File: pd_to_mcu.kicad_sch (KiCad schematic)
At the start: 0 parts

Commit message: updated UPD module
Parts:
- added C? (x2): 1u, symbol Device:C_Small
- added C? (x2): 2.2u, symbol Device:C_Small
- added D? (x2): D_TVS, Diode_SMD:D_1206_3216Metric_Pad1.42x1.75mm_HandSolder, symbol Device:D_TVS
- added J?: USB_C_Receptacle_USB2.0, symbol Connector:USB_C_Receptacle_USB2.0
- added R? (x3): R_US, symbol Device:R_US
- added U?: UPD350B28-QFN, symbol UPD:UPD350B28-QFN
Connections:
- new net: D?.1 (A1), J?.A6 (D+), J?.B6 (D+)
- new net: D?.1 (A1), J?.A7 (D-), J?.B7 (D-)
- new net: R?.2, U?. (VSW)
- new net +5V: J?.A4 (VBUS), J?.A9 (VBUS), J?.B4 (VBUS), J?.B9 (VBUS)
- new net 3V3_ALW: C?.2, U?. (VSW)
- new net D+: D?.2 (A2)
- new net D-: D?.2 (A2)
- new net Earth: C?.1, C?.1, C?.1, C?.1, J?.A1 (GND), J?.A12 (GND), J?.B1 (GND), J?.B12 (GND), J?.S1 (SHIELD), R?.1, U?. (VSW)
- new net VBUS: C?.2, R?.2, U?. (VSW)
- new net VBUS_DET: R?.1, R?.2, U?. (VSW)
- new net VDD18_CAP: C?.2, U?. (VSW)
- new net VDD33IO: R?.1, U?. (VSW)
- new net VSW: C?.2, U?. (VSW)

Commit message: update after meeting on tues
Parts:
- removed D? (x2): D_TVS, Diode_SMD:D_1206_3216Metric_Pad1.42x1.75mm_HandSolder, symbol Device:D_TVS
- added R?: R_US, symbol Device:R_US
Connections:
- net +5V is gone; now on net VBUS: J?.A4 (VBUS), J?.A9 (VBUS), J?.B4 (VBUS), J?.B9 (VBUS)
- net D+: now also J?.A6 (D+), J?.B6 (D+)
- net D-: now also J?.A7 (D-), J?.B7 (D-)
- net Earth: now also R?.1
- net CC1: now reaches J?.A5 (CC1)
- net CC1: now also U?. (VSW)
- net CC2: now reaches J?.B5 (CC2)
- net CC2: now also U?. (VSW)
- new net CFG_SEL: R?.2, U?. (VSW)
- new net VCONN: U?. (VSW)
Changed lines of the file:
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@@
+    (stroke (width 0) (type default) (color 0 0 0 0))
+  )
+  (wire (pts (xy 121.92 110.49) (xy 121.92 113.03))
+    (stroke (width 0) (type default) (color 0 0 0 0))
+  )
+  (wire (pts (xy 124.46 110.49) (xy 124.46 113.03))
+    (stroke (width 0) (type default) (color 0 0 0 0))
+  )
+  (wire (pts (xy 127 110.49) (xy 127 113.03))
     (stroke (width 0) (type default) (color 0 0 0 0))
   )
@@
     (stroke (width 0) (type default) (color 0 0 0 0))
   )
+  (wire (pts (xy 132.08 110.49) (xy 132.08 113.03))
+    (stroke (width 0) (type default) (color 0 0 0 0))
+  )
   (wire (pts (xy 144.78 87.63) (xy 147.32 87.63))
     (stroke (width 0) (type default) (color 0 0 0 0))
@@
     (stroke (width 0) (type default) (color 0 0 0 0))
   )
+  (wire (pts (xy 160.02 120.65) (xy 160.02 125.73))
+    (stroke (width 0) (type default) (color 0 0 0 0))
+  )
+  (wire (pts (xy 160.02 133.35) (xy 160.02 137.16))
+    (stroke (width 0) (type default) (color 0 0 0 0))
+  )
   (wire (pts (xy 167.64 74.93) (xy 171.45 74.93))
     (stroke (width 0) (type default) (color 0 0 0 0))
@@
     (stroke (width 0) (type default) (color 0 0 0 0))
   )
-  (wire (pts (xy 231.14 74.93) (xy 238.76 74.93))
-    (stroke (width 0) (type default) (color 0 0 0 0))
-  )
-  (wire (pts (xy 231.14 88.9) (xy 231.14 87.63))
-    (stroke (width 0) (type default) (color 0 0 0 0))
-  )
-  (wire (pts (xy 231.14 90.17) (xy 231.14 88.9))
-    (stroke (width 0) (type default) (color 0 0 0 0))
-  )
-  (wire (pts (xy 231.14 93.98) (xy 231.14 92.71))
-    (stroke (width 0) (type default) (color 0 0 0 0))
-  )
-  (wire (pts (xy 231.14 95.25) (xy 231.14 93.98))
+  (wire (pts (xy 231.14 74.93) (xy 236.22 74.93))
+    (stroke (width 0) (type default) (color 0 0 0 0))
+  )
+  (wire (pts (xy 231.14 80.01) (xy 236.22 80.01))
+    (stroke (width 0) (type default) (color 0 0 0 0))
+  )
+  (wire (pts (xy 231.14 82.55) (xy 236.22 82.55))
+    (stroke (width 0) (type default) (color 0 0 0 0))
+  )
+  (wire (pts (xy 231.14 87.63) (xy 231.14 88.9))
+    (stroke (width 0) (type default) (color 0 0 0 0))
+  )
+  (wire (pts (xy 231.14 88.9) (xy 231.14 90.17))
+    (stroke (width 0) (type default) (color 0 0 0 0))
+  )
+  (wire (pts (xy 231.14 88.9) (xy 233.68 88.9))
+    (stroke (width 0) (type default) (color 0 0 0 0))
+  )
+  (wire (pts (xy 231.14 92.71) (xy 231.14 93.98))
+    (stroke (width 0) (type default) (color 0 0 0 0))
+  )
+  (wire (pts (xy 231.14 93.98) (xy 231.14 95.25))
+    (stroke (width 0) (type default) (color 0 0 0 0))
+  )
+  (wire (pts (xy 231.14 93.98) (xy 233.68 93.98))
     (stroke (width 0) (type default) (color 0 0 0 0))
   )
@@
     )
   )
+  (global_label "CC2" (shape input) (at 121.92 113.03 270) (fields_autoplaced)
+    (effects (font (size 1.27 1.27)) (justify right))
+    (property "Intersheet References" "${INTERSHEET_REFS}" (id 0) (at 121.9994 119.1037 90)
+      (effects (font (size 1.27 1.27)) (justify right) hide)
+    )
+  )
+  (global_label "VCONN" (shape input) (at 124.46 113.03 270) (fields_autoplaced)
+    (effects (font (size 1.27 1.27)) (justify right))
+    (property "Intersheet References" "${INTERSHEET_REFS}" (id 0) (at 124.3806 121.7042 90)
+      (effects (font (size 1.27 1.27)) (justify right) hide)
+    )
+  )
+  (global_label "CC1" (shape input) (at 127 113.03 270) (fields_autoplaced)
+    (effects (font (size 1.27 1.27)) (justify right))
+    (property "Intersheet References" "${INTERSHEET_REFS}" (id 0) (at 127.0794 119.1037 90)
+      (effects (font (size 1.27 1.27)) (justify right) hide)
+    )
+  )
   (global_label "VBUS_DET" (shape input) (at 129.54 113.03 270) (fields_autoplaced)
     (effects (font (size 1.27 1.27)) (justify right))
@@
     )
   )
+  (global_label "CFG_SEL" (shape input) (at 132.08 113.03 270) (fields_autoplaced)
+    (effects (font (size 1.27 1.27)) (justify right))
+    (property "Intersheet References" "${INTERSHEET_REFS}" (id 0) (at 132.0006 123.3371 90)
+      (effects (font (size 1.27 1.27)) (justify right) hide)
+    )
+  )
   (global_label "VDD33IO" (shape input) (at 147.32 87.63 0) (fields_autoplaced)
     (effects (font (size 1.27 1.27)) (justify left))
@@
     )
   )
+  (global_label "CFG_SEL" (shape input) (at 160.02 120.65 90) (fields_autoplaced)
+    (effects (font (size 1.27 1.27)) (justify left))
+    (property "Intersheet References" "${INTERSHEET_REFS}" (id 0) (at 160.0994 110.3429 90)
+      (effects (font (size 1.27 1.27)) (justify left) hide)
+    )
+  )
   (global_label "VBUS_DET" (shape input) (at 171.45 74.93 0) (fields_autoplaced)
     (effects (font (size 1.27 1.27)) (justify left))
@@
     )
   )
-  (global_label "D-" (shape input) (at 238.76 88.9 0) (fields_autoplaced)
-    (effects (font (size 1.27 1.27)) (justify left))
-    (property "Intersheet References" "${INTERSHEET_REFS}" (id 0) (at 88.9 -16.51 0)
-      (effects (font (size 1.27 1.27)) hide)
-    )
-  )
-  (global_label "D+" (shape input) (at 238.76 93.98 0) (fields_autoplaced)
-    (effects (font (size 1.27 1.27)) (justify left))
-    (property "Intersheet References" "${INTERSHEET_REFS}" (id 0) (at 88.9 -16.51 0)
-      (effects (font (size 1.27 1.27)) hide)
-    )
-  )
-  (symbol (lib_id "power:+5V") (at 238.76 74.93 0) (unit 1)
-    (in_bom yes) (on_board yes)
-    (property "Reference" "#PWR?" (id 0) (at 238.76 78.74 0)
-      (effects (font (size 1.27 1.27)) hide)
-    )
-    (property "Value" "+5V" (id 1) (at 239.141 70.5358 0))
-    (property "Footprint" "" (id 2) (at 238.76 74.93 0)
-      (effects (font (size 1.27 1.27)) hide)
-    )
-    (property "Datasheet" "" (id 3) (at 238.76 74.93 0)
-      (effects (font (size 1.27 1.27)) hide)
-    )
-    (pin "1")
+  (global_label "D-" (shape input) (at 233.68 88.9 0) (fields_autoplaced)
+    (effects (font (size 1.27 1.27)) (justify left))
+    (property "Intersheet References" "${INTERSHEET_REFS}" (id 0) (at 83.82 -16.51 0)
+      (effects (font (size 1.27 1.27)) hide)
+    )
+  )
+  (global_label "D+" (shape input) (at 233.68 93.98 0) (fields_autoplaced)
+    (effects (font (size 1.27 1.27)) (justify left))
+    (property "Intersheet References" "${INTERSHEET_REFS}" (id 0) (at 83.82 -16.51 0)
+      (effects (font (size 1.27 1.27)) hide)
+    )
+  )
+  (global_label "VBUS" (shape input) (at 236.22 74.93 0) (fields_autoplaced)
+    (effects (font (size 1.27 1.27)) (justify left))
+    (property "Intersheet References" "${INTERSHEET_REFS}" (id 0) (at 243.4428 74.8506 0)
+      (effects (font (size 1.27 1.27)) (justify left) hide)
+    )
+  )
+  (global_label "CC1" (shape input) (at 236.22 80.01 0) (fields_autoplaced)
+    (effects (font (size 1.27 1.27)) (justify left))
+    (property "Intersheet References" "${INTERSHEET_REFS}" (id 0) (at 242.2937 79.9306 0)
+      (effects (font (size 1.27 1.27)) (justify left) hide)
+    )
+  )
+  (global_label "CC2" (shape input) (at 236.22 82.55 0) (fields_autoplaced)
+    (effects (font (size 1.27 1.27)) (justify left))
+    (property "Intersheet References" "${INTERSHEET_REFS}" (id 0) (at 242.2937 82.4706 0)
+      (effects (font (size 1.27 1.27)) (justify left) hide)
+    )
   )
   (symbol (lib_id "power:Earth") (at 64.77 115.57 0) (unit 1)
@@
     )
     (property "Datasheet" "~" (id 3) (at 137.16 110.49 0)
+      (effects (font (size 1.27 1.27)) hide)
+    )
+    (pin "1")
+  )
+  (symbol (lib_id "power:Earth") (at 160.02 137.16 0) (unit 1)
+    (in_bom yes) (on_board yes) (fields_autoplaced)
+    (property "Reference" "#PWR?" (id 0) (at 160.02 143.51 0)
+      (effects (font (size 1.27 1.27)) hide)
+    )
+    (property "Value" "Earth" (id 1) (at 160.02 140.97 0)
+      (effects (font (size 1.27 1.27)) hide)
+    )
+    (property "Footprint" "" (id 2) (at 160.02 137.16 0)
+      (effects (font (size 1.27 1.27)) hide)
+    )
+    (property "Datasheet" "~" (id 3) (at 160.02 137.16 0)
       (effects (font (size 1.27 1.27)) hide)
     )
@@
     )
     (property "Datasheet" "~" (id 3) (at 110.49 83.82 0)
+      (effects (font (size 1.27 1.27)) hide)
+    )
+    (pin "1")
+    (pin "2")
+  )
+  (symbol (lib_id "Device:R_US") (at 160.02 129.54 180) (unit 1)
+    (in_bom yes) (on_board yes) (fields_autoplaced)
+    (property "Reference" "R?" (id 0) (at 161.6711 128.6315 0)
+      (effects (font (size 1.27 1.27)) (justify right))
+    )
+    (property "Value" "R_US" (id 1) (at 161.6711 131.4066 0)
+      (effects (font (size 1.27 1.27)) (justify right))
+    )
+    (property "Footprint" "" (id 2) (at 159.004 129.286 90)
+      (effects (font (size 1.27 1.27)) hide)
+    )
+    (property "Datasheet" "~" (id 3) (at 160.02 129.54 0)
       (effects (font (size 1.27 1.27)) hide)
     )
@@
       (effects (font (size 1.27 1.27)) hide)
     )
-    (pin "1")
-    (pin "2")
-  )
-  (symbol (lib_id "Device:D_TVS") (at 234.95 88.9 0) (unit 1)
-    (in_bom yes) (on_board yes)
-    (property "Reference" "D?" (id 0) (at 234.95 83.3882 0))
-    (property "Value" "D_TVS" (id 1) (at 234.95 85.6996 0))
-    (property "Footprint" "Diode_SMD:D_1206_3216Metric_Pad1.42x1.75mm_HandSolder" (id 2) (at 234.95 88.9 0)
-      (effects (font (size 1.27 1.27)) hide)
-    )
-    (property "Datasheet" "~" (id 3) (at 234.95 88.9 0)
-      (effects (font (size 1.27 1.27)) hide)
-    )
-    (pin "1")
-    (pin "2")
-  )
-  (symbol (lib_id "Device:D_TVS") (at 234.95 93.98 0) (unit 1)
-    (in_bom yes) (on_board yes)
-    (property "Reference" "D?" (id 0) (at 234.95 96.52 0))
-    (property "Value" "D_TVS" (id 1) (at 234.95 99.06 0))
-    (property "Footprint" "Diode_SMD:D_1206_3216Metric_Pad1.42x1.75mm_HandSolder" (id 2) (at 234.95 93.98 0)
-      (effects (font (size 1.27 1.27)) hide)
-    )
-    (property "Datasheet" "~" (id 3) (at 234.95 93.98 0)
-      (effects (font (size 1.27 1.27)) hide)
-    )

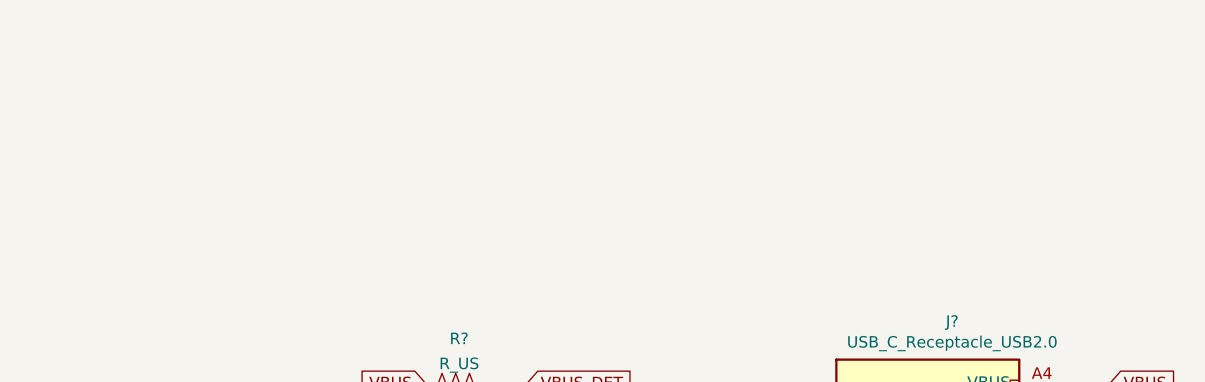
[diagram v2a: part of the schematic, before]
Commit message: added TODOs and comments
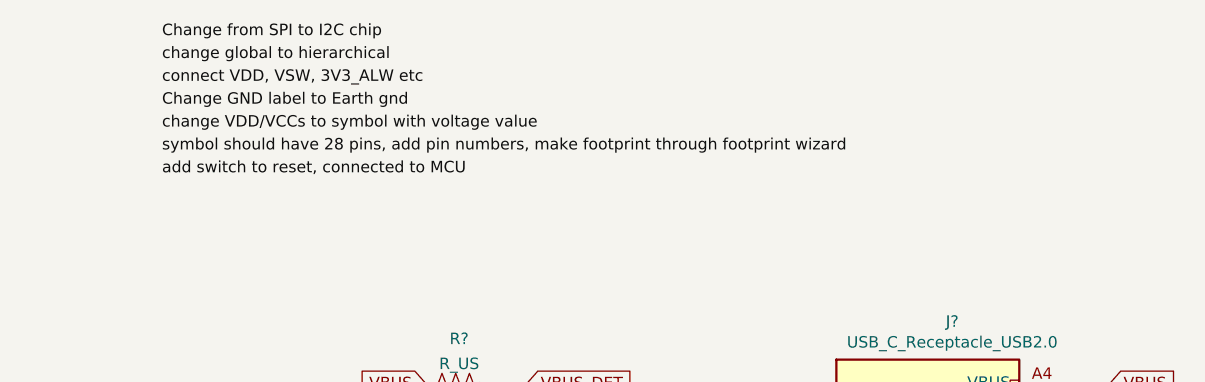
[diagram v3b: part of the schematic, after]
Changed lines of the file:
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@@
     (stroke (width 0) (type default) (color 0 0 0 0))
+  )
+  (label "Change from SPI to I2C chip" (at 130.81 36.83 0)
+    (effects (font (size 1.27 1.27)) (justify left bottom))
+  )
+  (label "change global to hierarchical" (at 130.81 39.37 0)
+    (effects (font (size 1.27 1.27)) (justify left bottom))
+  )
+  (label "connect VDD, VSW, 3V3_ALW etc" (at 130.81 41.91 0)
+    (effects (font (size 1.27 1.27)) (justify left bottom))
+  )
+  (label "Change GND label to Earth gnd" (at 130.81 44.45 0)
+    (effects (font (size 1.27 1.27)) (justify left bottom))
+  )
+  (label "change VDD{slash}VCCs to symbol with voltage value"
+    (at 130.81 46.99 0)
+    (effects (font (size 1.27 1.27)) (justify left bottom))
+  )
+  (label "symbol should have 28 pins, add pin numbers, make footprint through footprint wizard"
+    (at 130.81 49.53 0)
+    (effects (font (size 1.27 1.27)) (justify left bottom))
+  )
+  (label "add switch to reset, connected to MCU" (at 130.81 52.07 0)
+    (effects (font (size 1.27 1.27)) (justify left bottom))
   )
   (global_label "VDD18_CAP" (shape input) (at 74.93 81.28 0) (fields_autoplaced)

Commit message: updated UPD
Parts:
- removed C?: 2.2u, symbol Device:C_Small
- removed C?: 1u, symbol Device:C_Small
- U?: value UPD350B28-QFN -> UPD350A28-QFN
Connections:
- net CC1: now also U?.3 (CC1); no longer U?. (VSW)
- net CC2: now also U?.1 (CC2); no longer U?. (VSW)
- net CFG_SEL: now also U?.5 (CFG_SEL); no longer U?. (VSW)
- net Earth: now also U?.7 (PWR_DN); no longer U?. (VSW)
- net VBUS: now also U?.10 (3V3_VBUS), U?.8 (3V3_ALW); no longer U?. (VSW)
- net VBUS_DET: now also U?.4 (VBUS_DET); no longer U?. (VSW)
- net VCONN: now also U?.2 (VS); no longer U?. (VSW)
- net VSW: now also U?.11 (VDD18_CAP), U?.9 (VSW); no longer U?. (VSW)
- net at R?.2: no longer U?. (VSW)
- removed net 3V3_ALW: U?. (VSW)
- removed net VDD18_CAP: U?. (VSW)
- net VDD33IO renamed 3V3
- net 3V3: now also U?.12 (VDD33IO); no longer U?. (VSW)
- new net I2C_CLK_3V3: U?.14 (VDD_I2C)
- new net I2C_DAT_3V3: U?.13 (I2C_DAT)
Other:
- added sheet level_shifter_bidirectional (level_shifter_bidirectional_sch.kicad_sch)
- added sheet level_shifter_bidirectional1 (level_shifter_bidirectional_sch.kicad_sch)
- moved on the sheet: C?, J?

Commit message: updated schematic
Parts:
- added C? (x2): 1u, symbol Device:C_Small
- added D? (x3): LED_Small, symbol Device:LED_Small
- added U?: TPS7A0518PDBV, Package_TO_SOT_SMD:SOT-23-5, symbol Regulator_Linear:TPS7A0518PDBV
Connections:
- net Earth: now also C?.1, C?.1, D?.1 (K), D?.1 (K), D?.1 (K), U?.2 (GND)
- net I2C_CLK_3V3: now also U?.15 (I2C_CLK); no longer U?.14 (VDD_I2C)
- net +1V8: now reaches U?.20 (VDD18)
- net +1V8: now also C?.2, U?.5 (OUT)
- net ~{PD_IRQ}: now reaches U?.21 (IRQ_N)
- net ~{PD_RESET}: now reaches U?.22 (RESET_N)
- net ~{PD_RESET}: now also R?.2
- net at U?.26 (GPIO7): now also D?.2 (A)
- net at U?.27 (GPIO8): now also D?.2 (A)
- net at U?.28 (GPIO9): now also D?.2 (A)
- net 3V3: no longer names the net of U?.12 (VDD33IO)
- net 3V3: no longer R?.1
- new net +3V3: C?.2, R?.1, U?.1 (IN), U?.14 (VDD_I2C), U?.3 (EN)
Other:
- note added: "TVS Diodes on D+ D-"
- note added: "add resistors"
- moved on the sheet: C?, R?

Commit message: updated for winter 2022
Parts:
- removed R?: R_US, symbol Device:R_US
- added D? (x2): D_TVS, symbol Device:D_TVS
- added R? (x3): 5k, Resistor_SMD:R_0805_2012Metric_Pad1.20x1.40mm_HandSolder, symbol Device:R_US
- C11, C12, C13, C14: renamed from C?; footprint (none) -> Capacitor_SMD:C_0805_2012Metric_Pad1.18x1.45mm_HandSolder
- D1, D2, D3: renamed from D?; footprint (none) -> Diode_SMD:D_0805_2012Metric_Pad1.15x1.40mm_HandSolder
- J1: renamed from J?; footprint (none) -> Connector_USB:USB_C_Plug_JAE_DX07P024AJ1
- R5: renamed from R?; value R_US -> 90k; footprint (none) -> Resistor_SMD:R_0805_2012Metric_Pad1.20x1.40mm_HandSolder
- R6, R7: renamed from R?; value R_US -> 10k; footprint (none) -> Resistor_SMD:R_0805_2012Metric_Pad1.20x1.40mm_HandSolder
- U7: renamed from U?; footprint (none) -> Package_DFN_QFN:QFN-28-1EP_4x4mm_P0.4mm_EP2.4x2.4mm
- gave numbers to parts that had none: 1
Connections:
- net CFG_SEL is gone; now on net Earth: U7.5 (CFG_SEL)
- net D+: now also D?.2 (A2)
- net D-: now also D?.2 (A2)
- net Earth: now also D?.1 (A1), D?.1 (A1)
- net at D1.2 (A): now also R?.1; no longer U7.26 (GPIO7)
- net at D2.2 (A): now also R?.1; no longer U7.27 (GPIO8)
- net at U7.28 (GPIO9): now also R?.2; no longer D3.2 (A)
- new net: R?.2, U7.26 (GPIO7)
- new net: R?.2, U7.27 (GPIO8)
- new net: D3.2 (A), R?.1
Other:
- removed sheet level_shifter_bidirectional
- removed sheet level_shifter_bidirectional1
- note removed: "TVS Diodes on D+ D-"
- note removed: "add resistors"
- moved on the sheet: D1, D2, D3
